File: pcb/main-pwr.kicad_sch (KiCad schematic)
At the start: 30 parts, among them U2 ADP5054, U9 LM3880

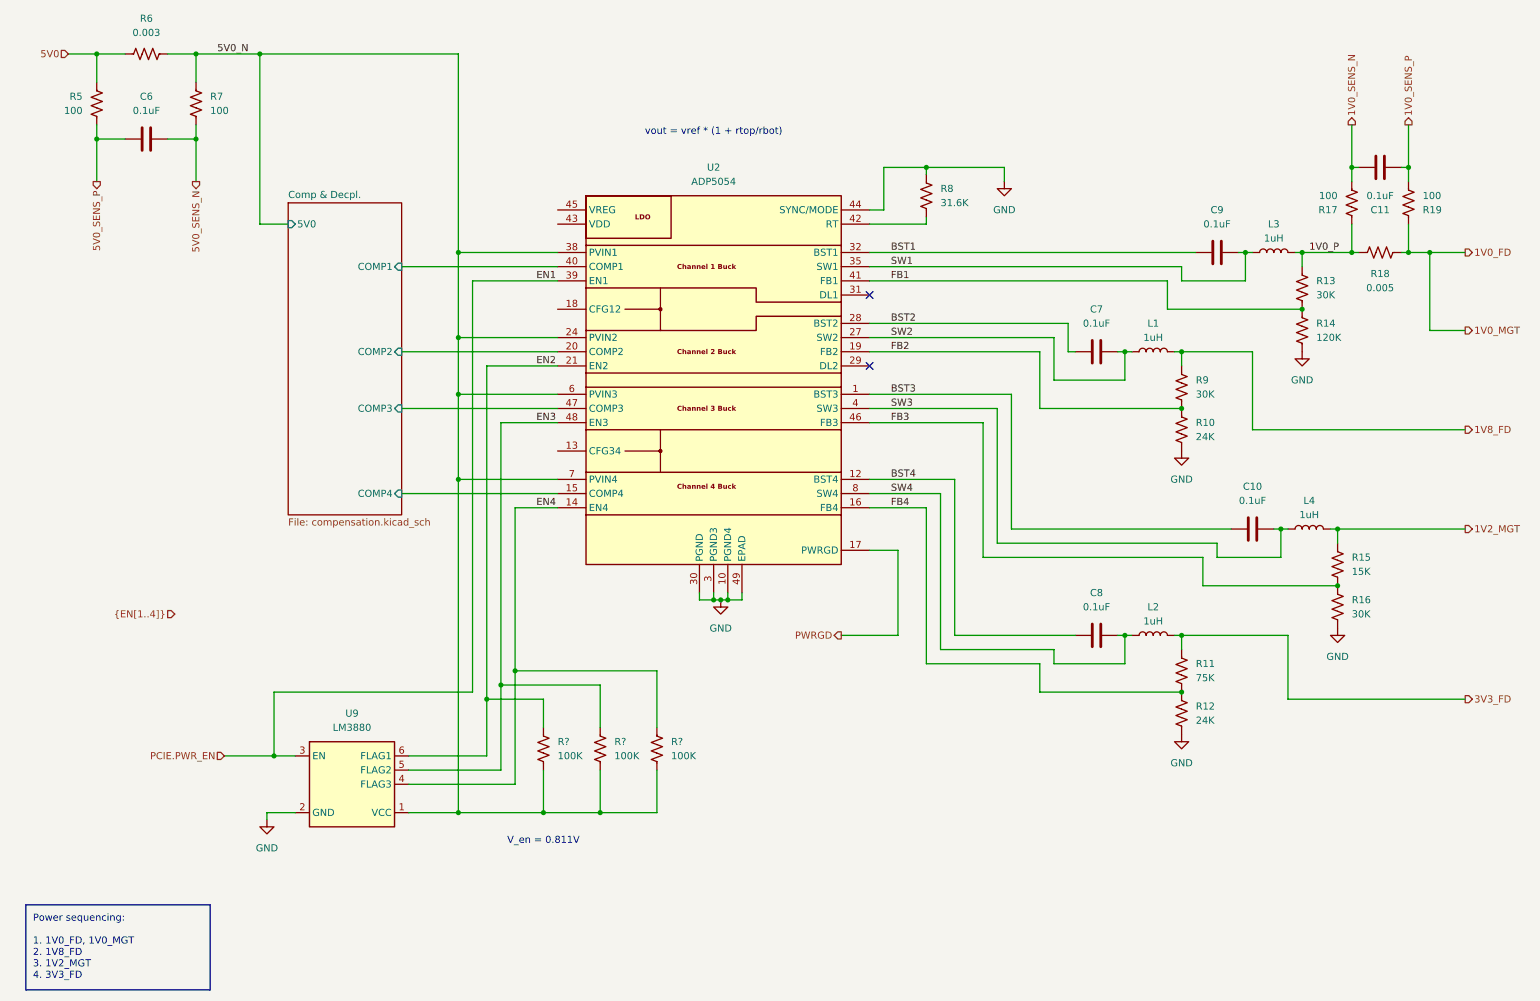
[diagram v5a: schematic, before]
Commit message: hierarchy and power sequencing, level shift
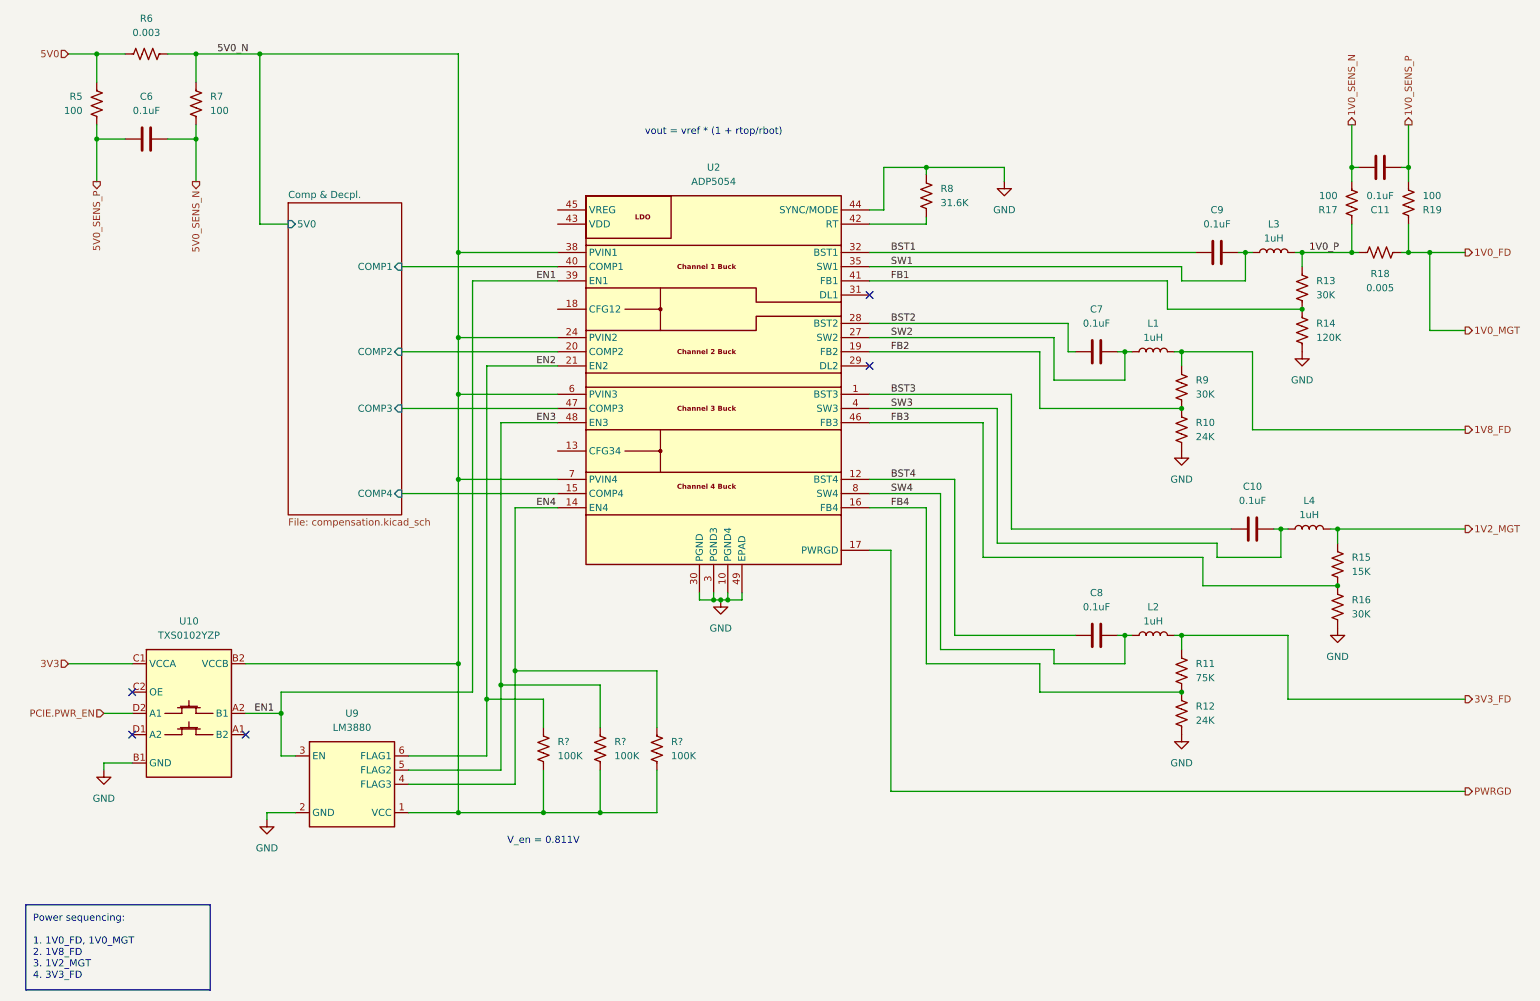
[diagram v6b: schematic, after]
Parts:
- added U10: TXS0102YZP, Package_BGA:Texas_DSBGA-8_0.9x1.9mm_Layout2x4_P0.5mm, symbol library:TXS0102YZP
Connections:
- net 5V0_N: now also U10.B2 (VCCB)
- net GND: now also U10.B1 (GND)
- net PCIE.PWR_EN: now also U10.D2 (A1); no longer U2.39 (EN1), U9.3 (EN)
- new net 3V3: U10.C1 (VCCA)
- new net EN1: U10.A2 (B1), U2.39 (EN1), U9.3 (EN)
- no-connect marks 2 -> 5

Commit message: added hierarchical sheet, pwr seq
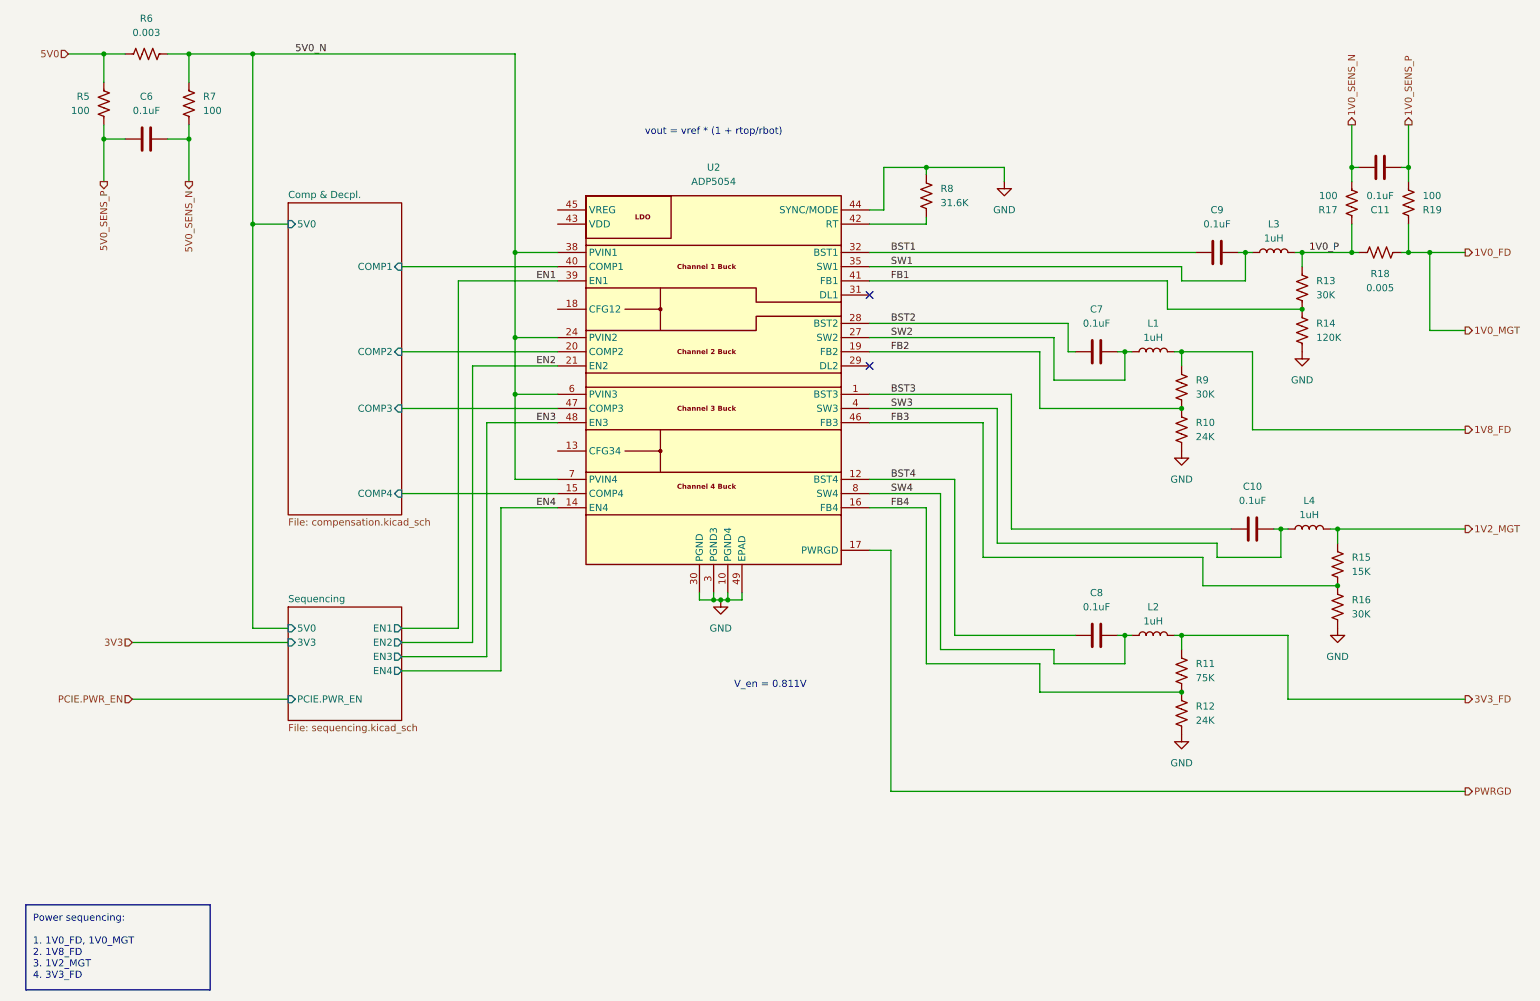
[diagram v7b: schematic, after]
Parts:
- removed R? (x3): 100K, symbol library:R_US
- removed U10: TXS0102YZP, Package_BGA:Texas_DSBGA-8_0.9x1.9mm_Layout2x4_P0.5mm, symbol library:TXS0102YZP
- removed U9: LM3880, Package_TO_SOT_SMD:SOT-23-6, symbol library:LM3880
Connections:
- no-connect marks 5 -> 2
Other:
- added sheet Sequencing (sequencing.kicad_sch)
- moved on the sheet: R5, R7

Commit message: defined memory pinouts
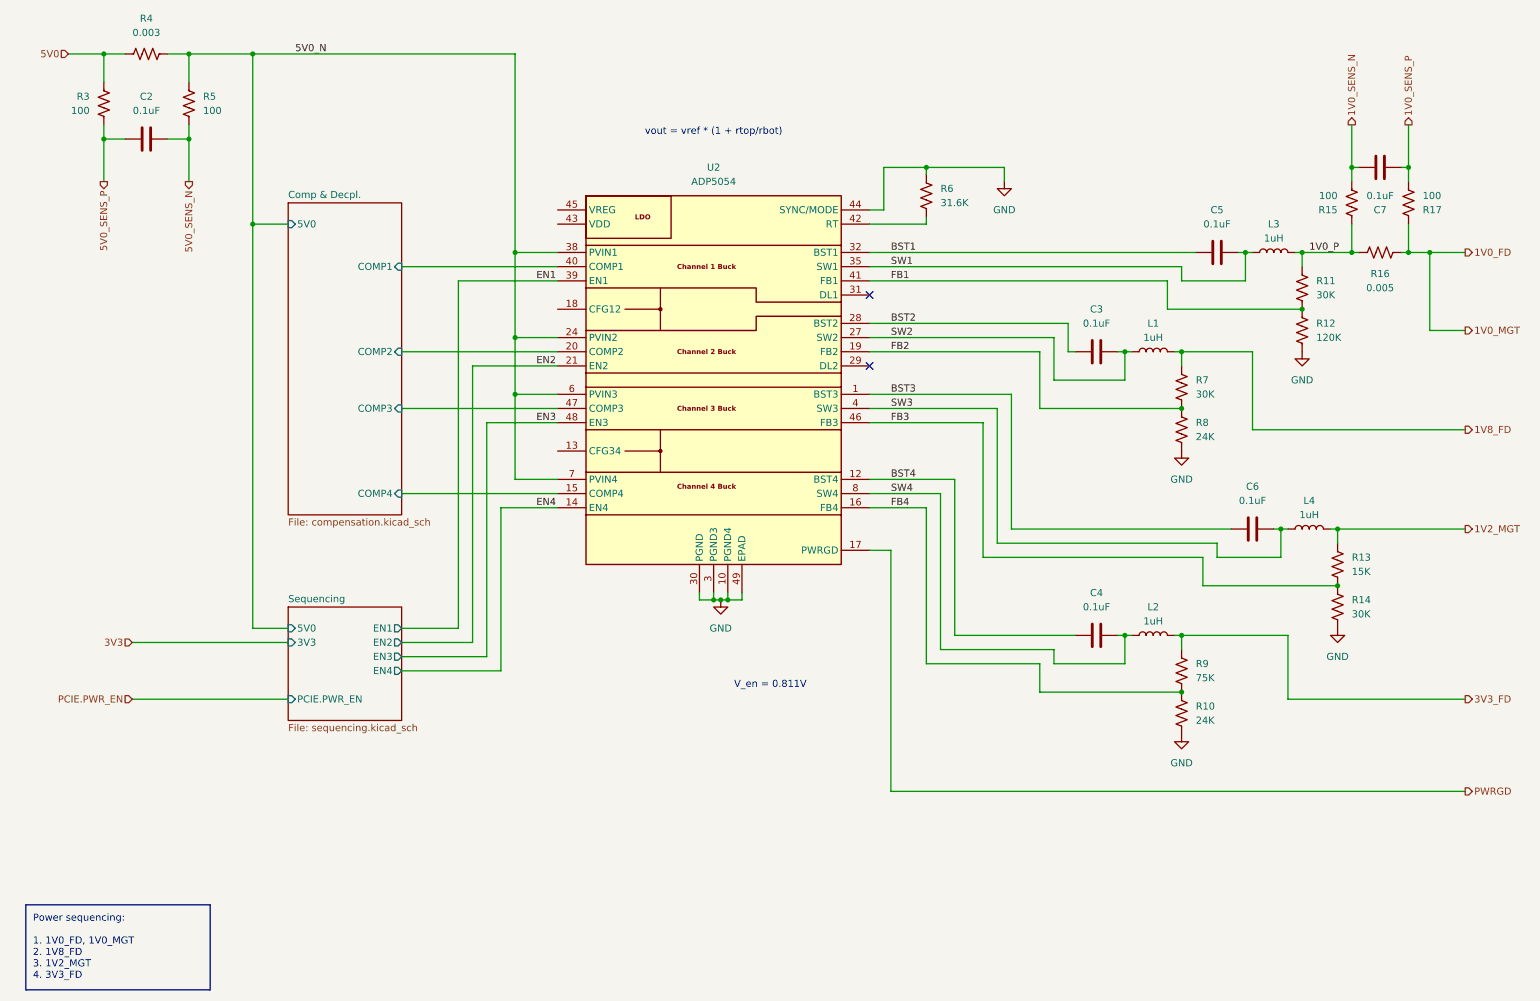
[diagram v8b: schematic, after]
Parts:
- renumbered C6 to C2, C7 to C3, C8 to C4, C9 to C5, C10 to C6, C11 to C7, R12 to R10, R13 to R11, R14 to R12, R15 to R13, R16 to R14, R17 to R15, R18 to R16, R19 to R17, R5 to R3, R6 to R4, R7 to R5, R8 to R6, R9 to R7, R10 to R8, R11 to R9
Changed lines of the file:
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@@
 		(dnp no)
 		(fields_autoplaced yes)
-		(property "Reference" "R14"
+		(property "Reference" "R12"
 			(at 246.38 74.9299 0)
 			(effects
@@
 			(project ""
 				(path "/e63e39d7-6ac0-4ffd-8aa3-1841a4541b55/f9ebb56c-78c7-42ac-bc19-ccbf788f5318"
-					(reference "R14")
+					(reference "R12")
 					(unit 1)
 				)
@@
 		(on_board yes)
 		(dnp no)
-		(property "Reference" "R18"
+		(property "Reference" "R16"
 			(at 257.81 66.04 90)
 			(effects
@@
 			(project "RPi-HwAB-1"
 				(path "/e63e39d7-6ac0-4ffd-8aa3-1841a4541b55/f9ebb56c-78c7-42ac-bc19-ccbf788f5318"
-					(reference "R18")
+					(reference "R16")
 					(unit 1)
 				)
@@
 		(dnp no)
 		(fields_autoplaced yes)
-		(property "Reference" "R16"
+		(property "Reference" "R14"
 			(at 252.73 124.4599 0)
 			(effects
@@
 			(project "RPi-HwAB-1"
 				(path "/e63e39d7-6ac0-4ffd-8aa3-1841a4541b55/f9ebb56c-78c7-42ac-bc19-ccbf788f5318"
-					(reference "R16")
+					(reference "R14")
 					(unit 1)
 				)
@@
 		(dnp no)
 		(fields_autoplaced yes)
-		(property "Reference" "C11"
+		(property "Reference" "C7"
 			(at 257.81 54.61 90)
 			(effects
@@
 			(project "RPi-HwAB-1"
 				(path "/e63e39d7-6ac0-4ffd-8aa3-1841a4541b55/f9ebb56c-78c7-42ac-bc19-ccbf788f5318"
-					(reference "C11")
+					(reference "C7")
 					(unit 1)
 				)
@@
 		(dnp no)
 		(fields_autoplaced yes)
-		(property "Reference" "#PWR020"
+		(property "Reference" "#PWR09"
 			(at 250.19 135.89 0)
 			(effects
@@
 			(project "RPi-HwAB-1"
 				(path "/e63e39d7-6ac0-4ffd-8aa3-1841a4541b55/f9ebb56c-78c7-42ac-bc19-ccbf788f5318"
-					(reference "#PWR020")
+					(reference "#PWR09")
 					(unit 1)
 				)
@@
 		(dnp no)
 		(fields_autoplaced yes)
-		(property "Reference" "R9"
+		(property "Reference" "R7"
 			(at 224.79 85.0899 0)
 			(effects
@@
 			(project "RPi-HwAB-1"
 				(path "/e63e39d7-6ac0-4ffd-8aa3-1841a4541b55/f9ebb56c-78c7-42ac-bc19-ccbf788f5318"
-					(reference "R9")
+					(reference "R7")
 					(unit 1)
 				)
@@
 		(dnp no)
 		(fields_autoplaced yes)
-		(property "Reference" "R15"
+		(property "Reference" "R13"
 			(at 252.73 116.8399 0)
 			(effects
@@
 			(project "RPi-HwAB-1"
 				(path "/e63e39d7-6ac0-4ffd-8aa3-1841a4541b55/f9ebb56c-78c7-42ac-bc19-ccbf788f5318"
-					(reference "R15")
+					(reference "R13")
 					(unit 1)
 				)
@@
 		(dnp no)
 		(fields_autoplaced yes)
-		(property "Reference" "R8"
+		(property "Reference" "R6"
 			(at 179.07 50.7999 0)
 			(effects
@@
 			(project ""
 				(path "/e63e39d7-6ac0-4ffd-8aa3-1841a4541b55/f9ebb56c-78c7-42ac-bc19-ccbf788f5318"
-					(reference "R8")
+					(reference "R6")
 					(unit 1)
 				)
@@
 		(dnp no)
 		(fields_autoplaced yes)
-		(property "Reference" "R10"
+		(property "Reference" "R8"
 			(at 224.79 92.7099 0)
 			(effects
@@
 			(project "RPi-HwAB-1"
 				(path "/e63e39d7-6ac0-4ffd-8aa3-1841a4541b55/f9ebb56c-78c7-42ac-bc19-ccbf788f5318"
-					(reference "R10")
+					(reference "R8")
 					(unit 1)
 				)
@@
 		(dnp no)
 		(fields_autoplaced yes)
-		(property "Reference" "C7"
+		(property "Reference" "C3"
 			(at 207.01 72.39 90)
 			(effects
@@
 			(project "RPi-HwAB-1"
 				(path "/e63e39d7-6ac0-4ffd-8aa3-1841a4541b55/f9ebb56c-78c7-42ac-bc19-ccbf788f5318"
-					(reference "C7")
+					(reference "C3")
 					(unit 1)
 				)
@@
 		(dnp no)
 		(fields_autoplaced yes)
-		(property "Reference" "#PWR019"
+		(property "Reference" "#PWR07"
 			(at 222.25 154.94 0)
 			(effects
@@
 			(project "RPi-HwAB-1"
 				(path "/e63e39d7-6ac0-4ffd-8aa3-1841a4541b55/f9ebb56c-78c7-42ac-bc19-ccbf788f5318"
-					(reference "#PWR019")
+					(reference "#PWR07")
 					(unit 1)
 				)
@@
 		(dnp no)
 		(fields_autoplaced yes)
-		(property "Reference" "R12"
+		(property "Reference" "R10"
 			(at 224.79 143.5099 0)
 			(effects
@@
 			(project "RPi-HwAB-1"
 				(path "/e63e39d7-6ac0-4ffd-8aa3-1841a4541b55/f9ebb56c-78c7-42ac-bc19-ccbf788f5318"
-					(reference "R12")
+					(reference "R10")
 					(unit 1)
 				)
@@
 		(dnp no)
 		(fields_autoplaced yes)
-		(property "Reference" "#PWR018"
+		(property "Reference" "#PWR06"
 			(at 222.25 104.14 0)
 			(effects
@@
 			(project "RPi-HwAB-1"
 				(path "/e63e39d7-6ac0-4ffd-8aa3-1841a4541b55/f9ebb56c-78c7-42ac-bc19-ccbf788f5318"
-					(reference "#PWR018")
+					(reference "#PWR06")
 					(unit 1)
 				)
@@
 		(dnp no)
 		(fields_autoplaced yes)
-		(property "Reference" "R11"
+		(property "Reference" "R9"
 			(at 224.79 135.8899 0)
 			(effects
@@
 			(project "RPi-HwAB-1"
 				(path "/e63e39d7-6ac0-4ffd-8aa3-1841a4541b55/f9ebb56c-78c7-42ac-bc19-ccbf788f5318"
-					(reference "R11")
+					(reference "R9")
 					(unit 1)
 				)
@@
 		(dnp no)
 		(fields_autoplaced yes)
-		(property "Reference" "R6"
+		(property "Reference" "R4"
 			(at 36.83 20.32 90)
 			(effects
@@
 			(project ""
 				(path "/e63e39d7-6ac0-4ffd-8aa3-1841a4541b55/f9ebb56c-78c7-42ac-bc19-ccbf788f5318"
-					(reference "R6")
+					(reference "R4")
 					(unit 1)
 				)
@@
 		(dnp no)
 		(fields_autoplaced yes)
-		(property "Reference" "R7"
+		(property "Reference" "R5"
 			(at 46.99 34.2899 0)
 			(effects
@@
 			(project "RPi-HwAB-1"
 				(path "/e63e39d7-6ac0-4ffd-8aa3-1841a4541b55/f9ebb56c-78c7-42ac-bc19-ccbf788f5318"
-					(reference "R7")
+					(reference "R5")
 					(unit 1)
 				)
@@
 		(dnp no)
 		(fields_autoplaced yes)
-		(property "Reference" "C10"
+		(property "Reference" "C6"
 			(at 234.95 104.14 90)
 			(effects
@@
 			(project "RPi-HwAB-1"
 				(path "/e63e39d7-6ac0-4ffd-8aa3-1841a4541b55/f9ebb56c-78c7-42ac-bc19-ccbf788f5318"
-					(reference "C10")
+					(reference "C6")
 					(unit 1)
 				)
@@
 		(on_board yes)
 		(dnp no)
-		(property "Reference" "R5"
+		(property "Reference" "R3"
 			(at 26.67 34.29 0)
 			(effects
@@
 			(project ""
 				(path "/e63e39d7-6ac0-4ffd-8aa3-1841a4541b55/f9ebb56c-78c7-42ac-bc19-ccbf788f5318"
-					(reference "R5")
+					(reference "R3")
 					(unit 1)
 				)
@@
 		(on_board yes)
 		(dnp no)
-		(property "Reference" "R19"
+		(property "Reference" "R17"
 			(at 265.43 54.61 0)
 			(effects
@@
 			(project "RPi-HwAB-1"
 				(path "/e63e39d7-6ac0-4ffd-8aa3-1841a4541b55/f9ebb56c-78c7-42ac-bc19-ccbf788f5318"
-					(reference "R19")
+					(reference "R17")
 					(unit 1)
 				)
@@
 		(dnp no)
 		(fields_autoplaced yes)
-		(property "Reference" "C6"
+		(property "Reference" "C2"
 			(at 36.83 34.29 90)
 			(effects
@@
 			(project ""
 				(path "/e63e39d7-6ac0-4ffd-8aa3-1841a4541b55/f9ebb56c-78c7-42ac-bc19-ccbf788f5318"
-					(reference "C6")
+					(reference "C2")
 					(unit 1)
 				)
@@
 		(dnp no)
 		(fields_autoplaced yes)
-		(property "Reference" "#PWR09"
+		(property "Reference" "#PWR04"
 			(at 139.7 130.81 0)
 			(effects
@@
 			(project ""
 				(path "/e63e39d7-6ac0-4ffd-8aa3-1841a4541b55/f9ebb56c-78c7-42ac-bc19-ccbf788f5318"
-					(reference "#PWR09")
+					(reference "#PWR04")
 					(unit 1)
 				)
@@
 		(on_board yes)
 		(dnp no)
-		(property "Reference" "C9"
+		(property "Reference" "C5"
 			(at 228.6 54.61 90)
 			(effects
@@
 			(project ""
 				(path "/e63e39d7-6ac0-4ffd-8aa3-1841a4541b55/f9ebb56c-78c7-42ac-bc19-ccbf788f5318"
-					(reference "C9")
+					(reference "C5")
 					(unit 1)
 				)
@@
 		(dnp no)
 		(fields_autoplaced yes)
-		(property "Reference" "#PWR010"
+		(property "Reference" "#PWR05"
 			(at 190.5 55.88 0)
 			(effects
@@
 			(project ""
 				(path "/e63e39d7-6ac0-4ffd-8aa3-1841a4541b55/f9ebb56c-78c7-42ac-bc19-ccbf788f5318"
-					(reference "#PWR010")
+					(reference "#PWR05")
 					(unit 1)
 				)
@@
 		(dnp no)
 		(fields_autoplaced yes)
-		(property "Reference" "C8"
+		(property "Reference" "C4"
 			(at 207.01 123.19 90)
 			(effects
@@
 			(project "RPi-HwAB-1"
 				(path "/e63e39d7-6ac0-4ffd-8aa3-1841a4541b55/f9ebb56c-78c7-42ac-bc19-ccbf788f5318"
-					(reference "C8")
+					(reference "C4")
 					(unit 1)
 				)
@@
 		(dnp no)
 		(fields_autoplaced yes)
-		(property "Reference" "#PWR017"
+		(property "Reference" "#PWR08"
 			(at 243.84 86.36 0)
 			(effects
@@
 			(project "RPi-HwAB-1"
 				(path "/e63e39d7-6ac0-4ffd-8aa3-1841a4541b55/f9ebb56c-78c7-42ac-bc19-ccbf788f5318"
-					(reference "#PWR017")
+					(reference "#PWR08")
 					(unit 1)
 				)
@@
 		(dnp no)
 		(fields_autoplaced yes)
-		(property "Reference" "R13"
+		(property "Reference" "R11"
 			(at 246.38 67.3099 0)
 			(effects
@@
 			(project "RPi-HwAB-1"
 				(path "/e63e39d7-6ac0-4ffd-8aa3-1841a4541b55/f9ebb56c-78c7-42ac-bc19-ccbf788f5318"
-					(reference "R13")
+					(reference "R11")
 					(unit 1)
 				)
@@
 		(dnp no)
 		(fields_autoplaced yes)
-		(property "Reference" "R17"
+		(property "Reference" "R15"
 			(at 250.19 54.6101 0)
 			(effects
@@
 			(project "RPi-HwAB-1"
 				(path "/e63e39d7-6ac0-4ffd-8aa3-1841a4541b55/f9ebb56c-78c7-42ac-bc19-ccbf788f5318"
-					(reference "R17")
+					(reference "R15")
 					(unit 1)
 				)
@@
 			(project "RPi-HwAB-1"
 				(path "/e63e39d7-6ac0-4ffd-8aa3-1841a4541b55/f9ebb56c-78c7-42ac-bc19-ccbf788f5318"
-					(page "13")
+					(page "4")
 				)
 			)
@@
 			(project "RPi-HwAB-1"
 				(path "/e63e39d7-6ac0-4ffd-8aa3-1841a4541b55/f9ebb56c-78c7-42ac-bc19-ccbf788f5318"
-					(page "12")
-				)
-			)
+					(page "3")
+				)
+			)
